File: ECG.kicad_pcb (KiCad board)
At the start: 4 copper layers, 60 x 60 mm, 98 parts, among them J1 SJ-3566AN, J2 Conn_01x02_Male, J3 Conn_01x08_Male, J4 Conn_01x02_Male, J5 Conn_ARM_JTAG_SWD_10, Q1 BC858, U1 ADR4525, U2 LTC3531, U3 INA333, U4 OPA388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

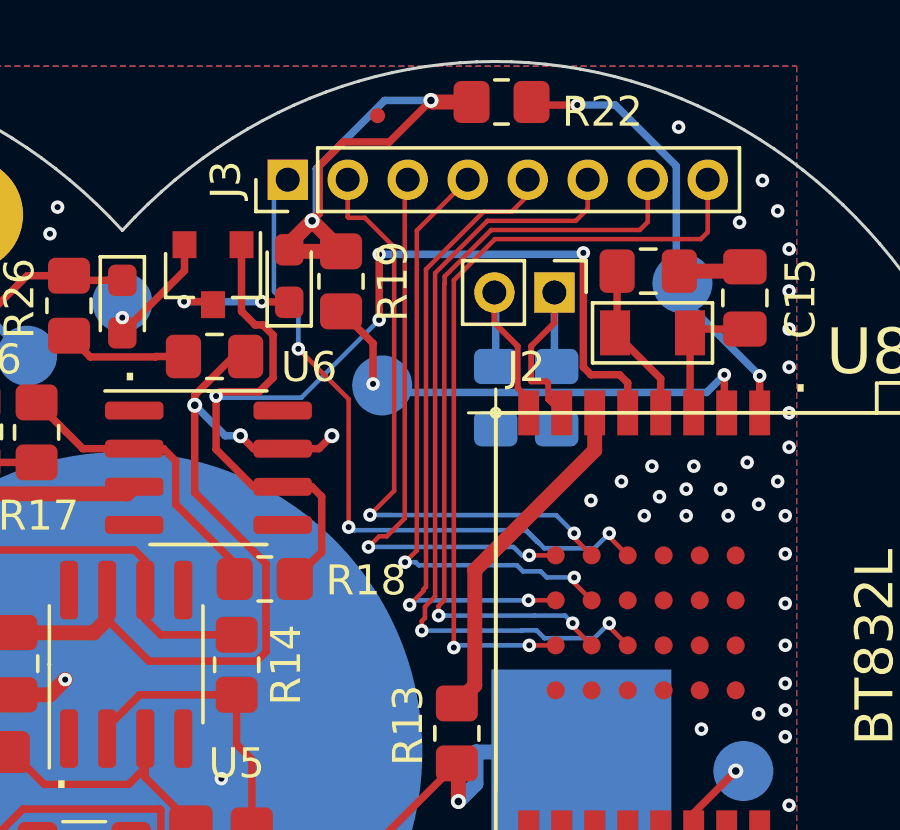
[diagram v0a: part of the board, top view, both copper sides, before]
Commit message: Fixed power and ground pours
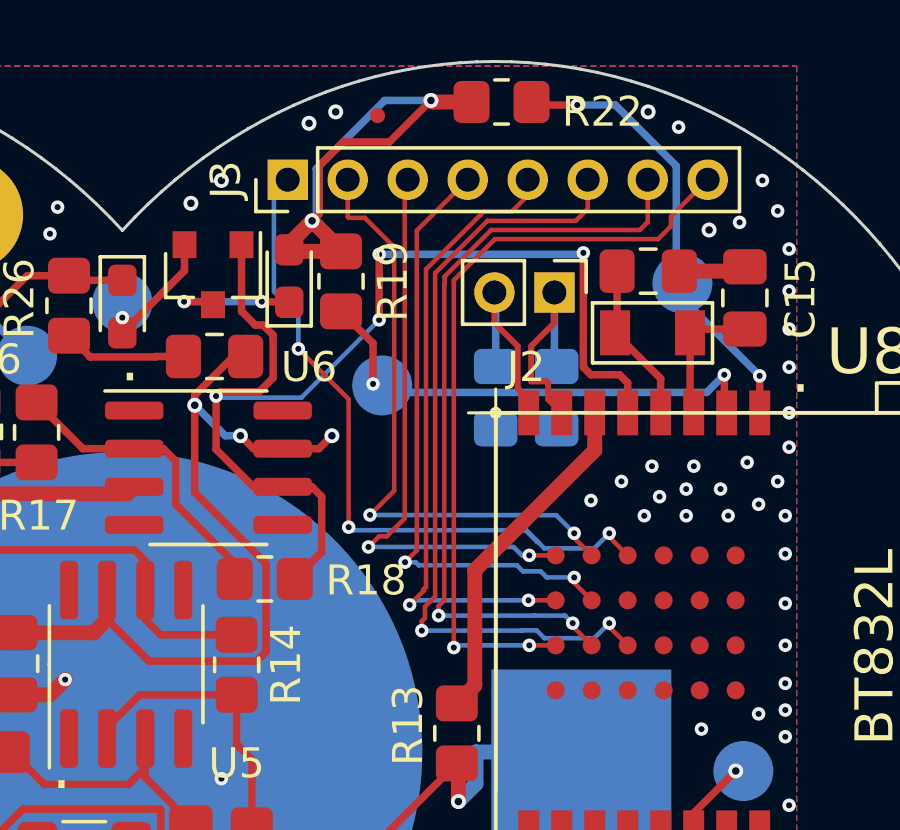
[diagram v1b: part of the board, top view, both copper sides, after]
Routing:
- net (no net): track 11.5 -> 0.00 mm
- net 3.3V: track 123.1 -> 133.7 mm, vias 25 -> 29
- net GND: track 35.4 -> 42.5 mm, vias 164 -> 166
- net Net-(J3-Pad8): track 26.5 -> 25.7 mm

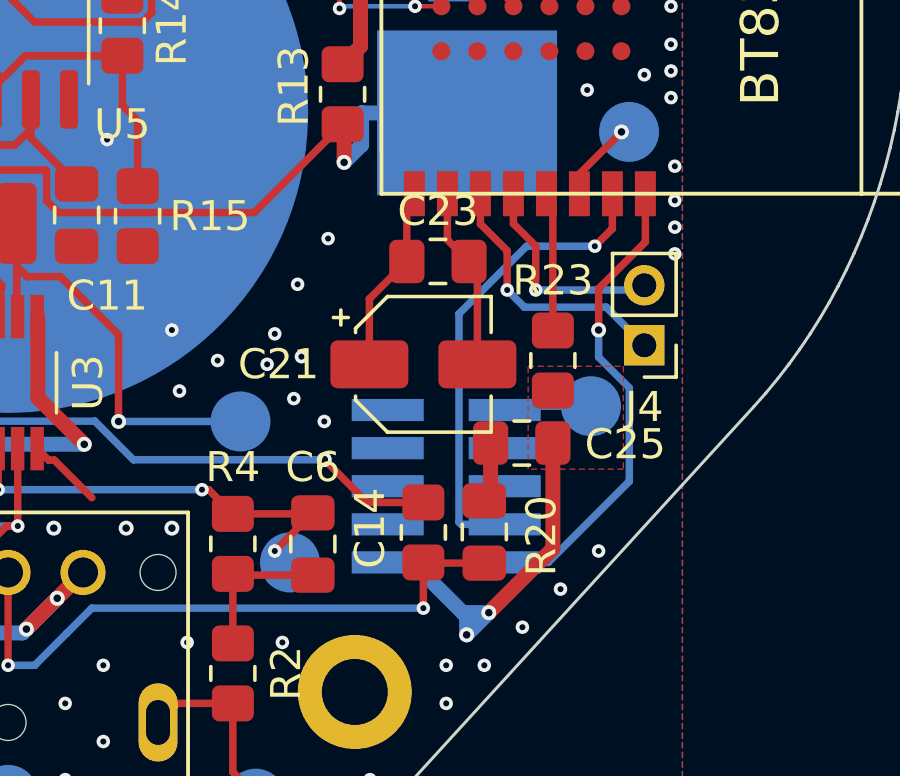
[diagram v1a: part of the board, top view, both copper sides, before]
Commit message: Updated ground pour and fixed C23 silkscreen
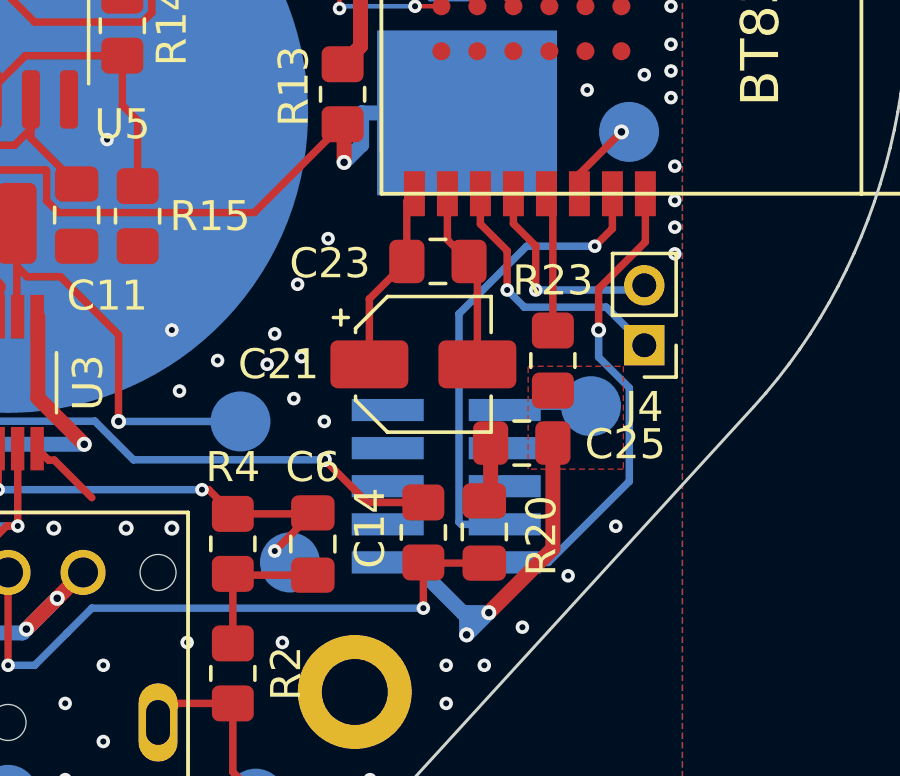
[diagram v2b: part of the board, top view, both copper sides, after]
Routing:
- net GND: vias 166 -> 168
- net (no net): vias 2 -> 0
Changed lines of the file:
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@@
-(kicad_pcb (version 20171130) (host pcbnew 5.1.8)
+(kicad_pcb (version 20171130) (host pcbnew 5.1.5+dfsg1-2build2)
   (general
     (thickness 1.6)
@@
   )
   (setup
-    (last_trace_width 0.5)
+    (last_trace_width 0.25)
     (user_trace_width 0.1524)
     (user_trace_width 0.5)
@@
     (tags "capacitor handsolder")
     (attr smd)
-    (fp_text reference C23 (at 0 -1.68) (layer F.SilkS)
+    (fp_text reference C23 (at -3.598 0.0635) (layer F.SilkS)
       (effects (font (size 1 1) (thickness 0.15)))
     )
@@
   (gr_line (start 122.363821 94.7375) (end 122.363821 94.7375) (layer Edge.Cuts) (width 0.1))
   (gr_line (start 122.363821 94.7375) (end 122.363821 94.7375) (layer Edge.Cuts) (width 0.1))
-  (via (at 170.18 119.38) (size 0.45) (drill 0.2) (layers F.Cu B.Cu) (net 0))
-  (via (at 171.45 118.11) (size 0.45) (drill 0.2) (layers F.Cu B.Cu) (net 0))
-  (via (at 169.291 82.169) (size 0.5) (drill 0.25) (layers F.Cu B.Cu) (net 45))
-  (via (at 171.323 86.106) (size 0.5) (drill 0.25) (layers F.Cu B.Cu) (net 45))
   (via (at 137.16 105.41) (size 0.45) (drill 0.2) (layers F.Cu B.Cu) (net 1))
   (via (at 134.62 105.41) (size 0.45) (drill 0.2) (layers F.Cu B.Cu) (net 1))
@@
   (segment (start 158.301153 83.202401) (end 156.050414 83.202401) (width 0.5) (layer Gnd.Cu) (net 2))
   (segment (start 158.877 82.169) (end 158.877 82.626554) (width 0.5) (layer Gnd.Cu) (net 2))
-  (via (at 155.067 84.455) (size 0.5) (drill 0.25) (layers F.Cu B.Cu) (net 45))
+  (via (at 172.0215 117.2845) (size 0.45) (drill 0.2) (layers F.Cu B.Cu) (net 2))
+  (via (at 170.434 118.9355) (size 0.45) (drill 0.2) (layers F.Cu B.Cu) (net 2))
   (segment (start 138.025 117.475) (end 139 117.475) (width 0.5) (layer F.Cu) (net 3))
   (segment (start 136.525 115.975) (end 138.025 117.475) (width 0.5) (layer F.Cu) (net 3))
@@
   (segment (start 139.065 85.852) (end 137.795 87.122) (width 0.25) (layer B.Cu) (net 30))
   (segment (start 139.065 84.455) (end 139.065 85.852) (width 0.25) (layer B.Cu) (net 30))
+  (via (at 169.291 82.169) (size 0.5) (drill 0.25) (layers F.Cu B.Cu) (net 45))
+  (via (at 171.323 86.106) (size 0.5) (drill 0.25) (layers F.Cu B.Cu) (net 45))
+  (via (at 155.067 84.455) (size 0.5) (drill 0.25) (layers F.Cu B.Cu) (net 45))
   (via (at 141.859 88.646) (size 0.45) (drill 0.2) (layers F.Cu B.Cu) (net 45))
   (via (at 140.462 88.646) (size 0.45) (drill 0.2) (layers F.Cu B.Cu) (net 45))

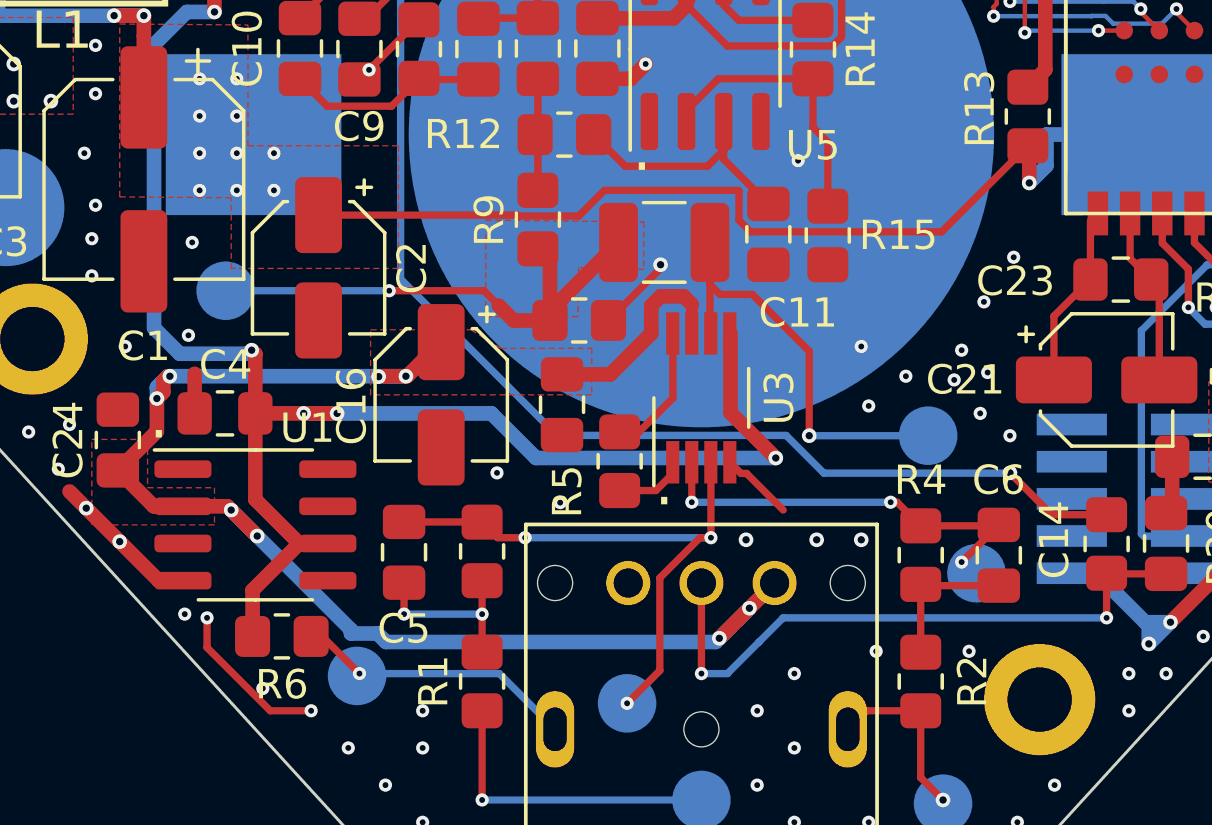
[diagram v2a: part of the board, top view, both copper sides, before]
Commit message: #21 - Hook up switch to battery line
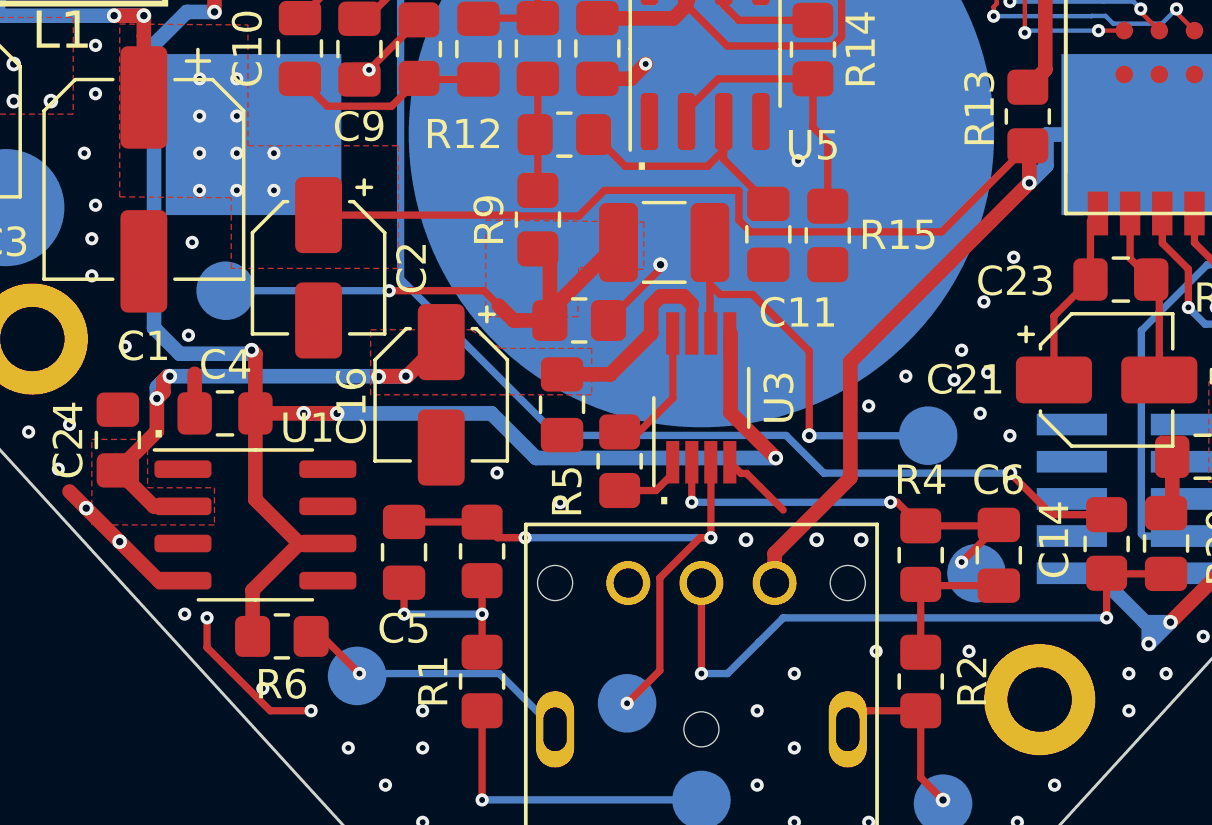
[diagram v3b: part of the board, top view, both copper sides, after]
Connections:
- J1 pad 6: 3.3V -> Vbatt
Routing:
- net 3.3V: track 133.7 -> 108.0 mm, vias 29 -> 25
- net Vbatt: track 46.7 -> 64.0 mm
- net GND: vias 168 -> 167

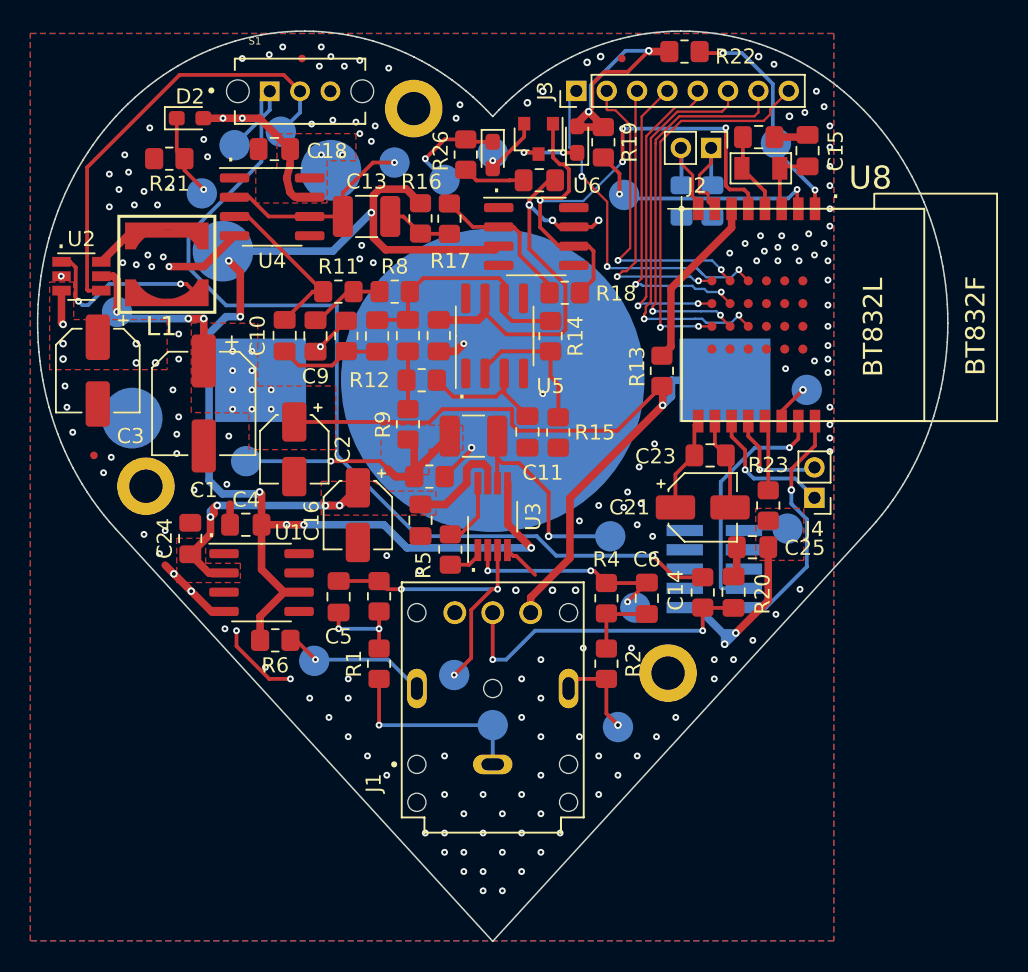
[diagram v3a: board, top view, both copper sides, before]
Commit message: #19 and #20 - Fix the micro debug and power connections
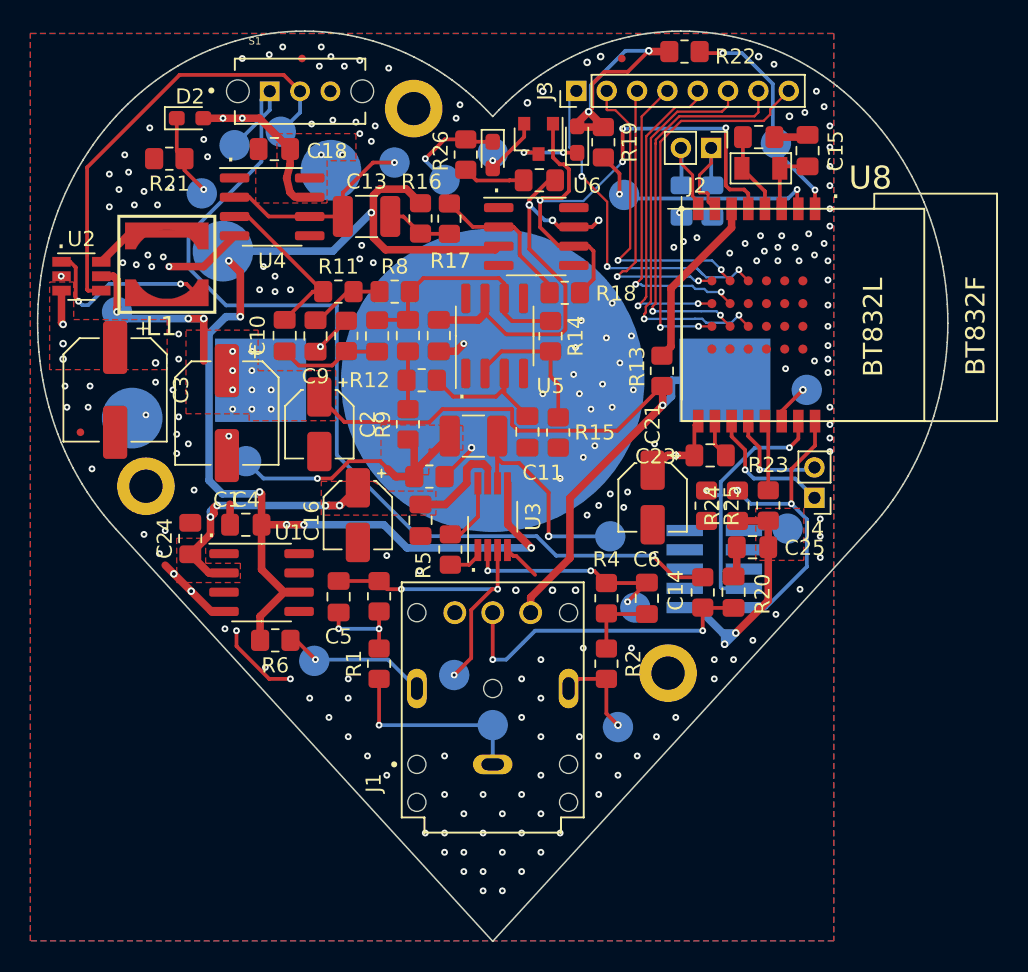
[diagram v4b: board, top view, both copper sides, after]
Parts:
- added R24: 100k, Resistor_SMD:R_0805_2012Metric_Pad1.20x1.40mm_HandSolder, F.Cu at (167.9, 111.8)
- added R25: 100k, Resistor_SMD:R_0805_2012Metric_Pad1.20x1.40mm_HandSolder, F.Cu at (165.9, 111.8)
- C3: footprint Capacitor_SMD:CP_Elec_5x5.3 -> Capacitor_SMD:CP_Elec_6.3x5.3
- moved C21 3.37 mm to (162.3, 111.2), turned to 270 degrees
- moved C2 2.33 mm to (140.3, 106.4)
- moved REF** 1.76 mm to (124.6, 106.9)
- moved C3 1.71 mm to (126.9, 104.1)
- moved C1 1.65 mm to (134.2, 105.7)
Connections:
- C21 pad 1: Net-(C21-Pad1) -> 3.3V
- C21 pad 2: Net-(C21-Pad2) -> GND
- C23 pad 1: Net-(C21-Pad1) -> 3.3V
- C23 pad 2: Net-(C21-Pad2) -> GND
- U8 pad P$10: Net-(C21-Pad2) -> GND
- U8 pad P$9: Net-(C21-Pad1) -> 3.3V
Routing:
- net 3.3V: track 108.0 -> 117.3 mm, vias 25 -> 24
- net Net-(C21-Pad1): track 6.31 -> 0.00 mm
- net Net-(C21-Pad2): track 6.10 -> 0.00 mm
- net Net-(J5-Pad2): track 15.9 -> 19.8 mm, vias 1 -> 2
- net GND: track 42.5 -> 45.4 mm, vias 167 -> 193
- net Net-(J5-Pad4): track 16.0 -> 17.0 mm, vias 1 -> 2
- net Vbatt: track 64.0 -> 63.0 mm
- net /Filters_And_Gain/Vin: track 17.8 -> 18.7 mm

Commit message: #22 - Detach battery ADC while the micro is not powered
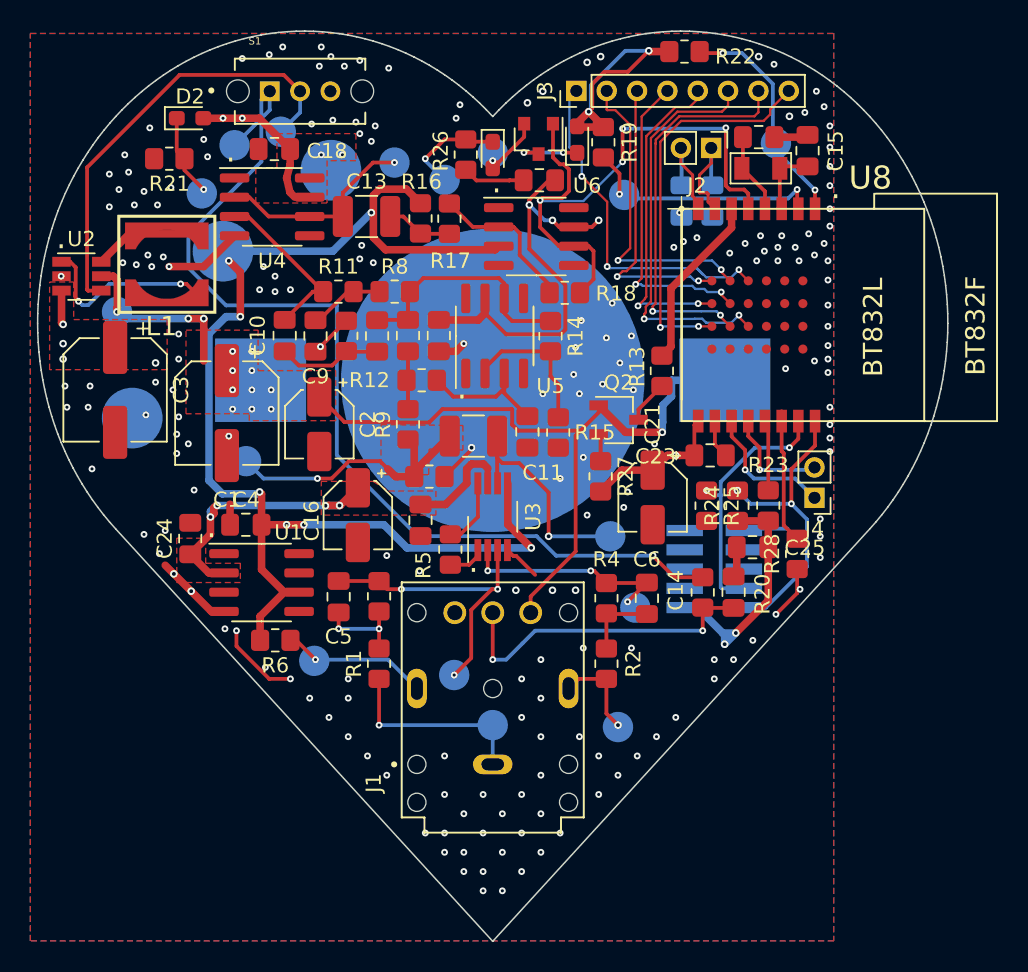
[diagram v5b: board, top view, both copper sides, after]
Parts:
- removed REF** (x3): MountingHole_2.2mm_M2_DIN965_Pad, MountingHole:MountingHole_2.2mm_M2_DIN965_Pad
- removed REF** (x3): Fiducial_0.5mm_Mask1.5mm, Fiducial:Fiducial_0.5mm_Mask1.5mm
- removed TP14, TP22: TestPoint, TestPoint:TestPoint_Pad_D2.0mm
- added Q2: Q_NMOS_DGS, Package_TO_SOT_SMD:TSOT-23, F.Cu at (160.1, 106.1)
- added R27: 100, Resistor_SMD:R_0805_2012Metric_Pad1.20x1.40mm_HandSolder, F.Cu at (158.9, 109.8)
- added R28: 2k, Resistor_SMD:R_0805_2012Metric_Pad1.20x1.40mm_HandSolder, F.Cu at (171.8, 115.0)
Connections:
- R13 pad 2: Vbatt -> Net-(Q2-Pad3)
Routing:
- net Net-(R28-Pad2): track 2.64 -> 8.83 mm, vias 1 -> 0
- net 3.3V: track 117.3 -> 121.3 mm
- net GND: track 45.4 -> 49.0 mm, vias 193 -> 188
- net Net-(Q2-Pad3): track 0.00 -> 2.94 mm
- net Vbatt: track 63.0 -> 60.1 mm
- net Net-(Q2-Pad2): track 0.00 -> 1.83 mm
